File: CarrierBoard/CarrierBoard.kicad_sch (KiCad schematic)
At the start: 5 parts, among them J1 5-520315-4, J2 5-520315-6, J3 5-520315-8, J4 05JQ-BT, J5 09JQ-BT

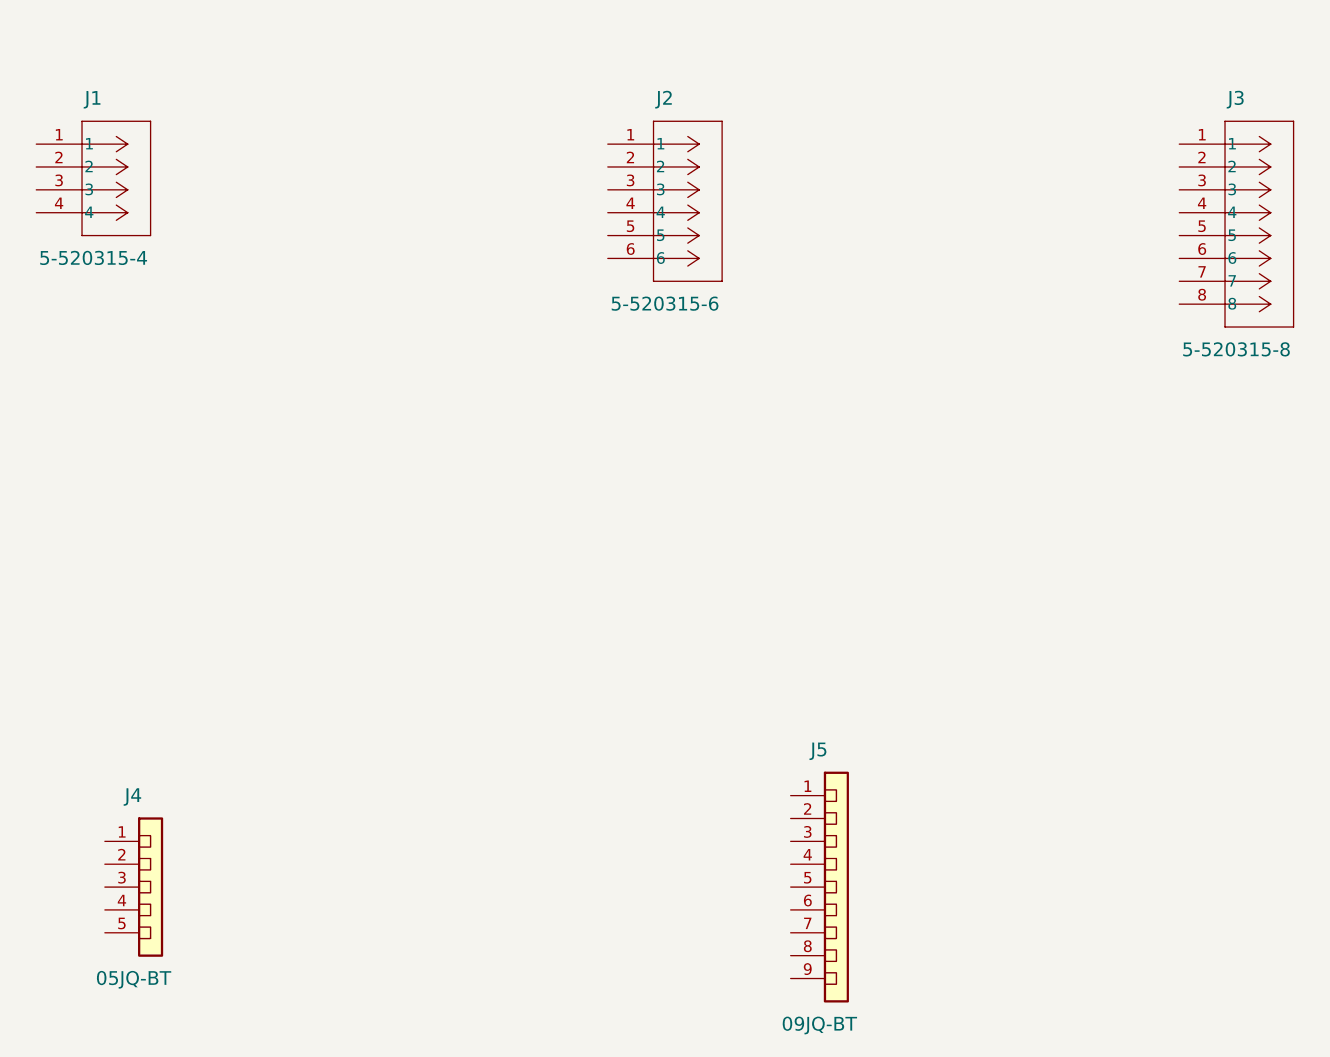
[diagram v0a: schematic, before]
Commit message: power flags
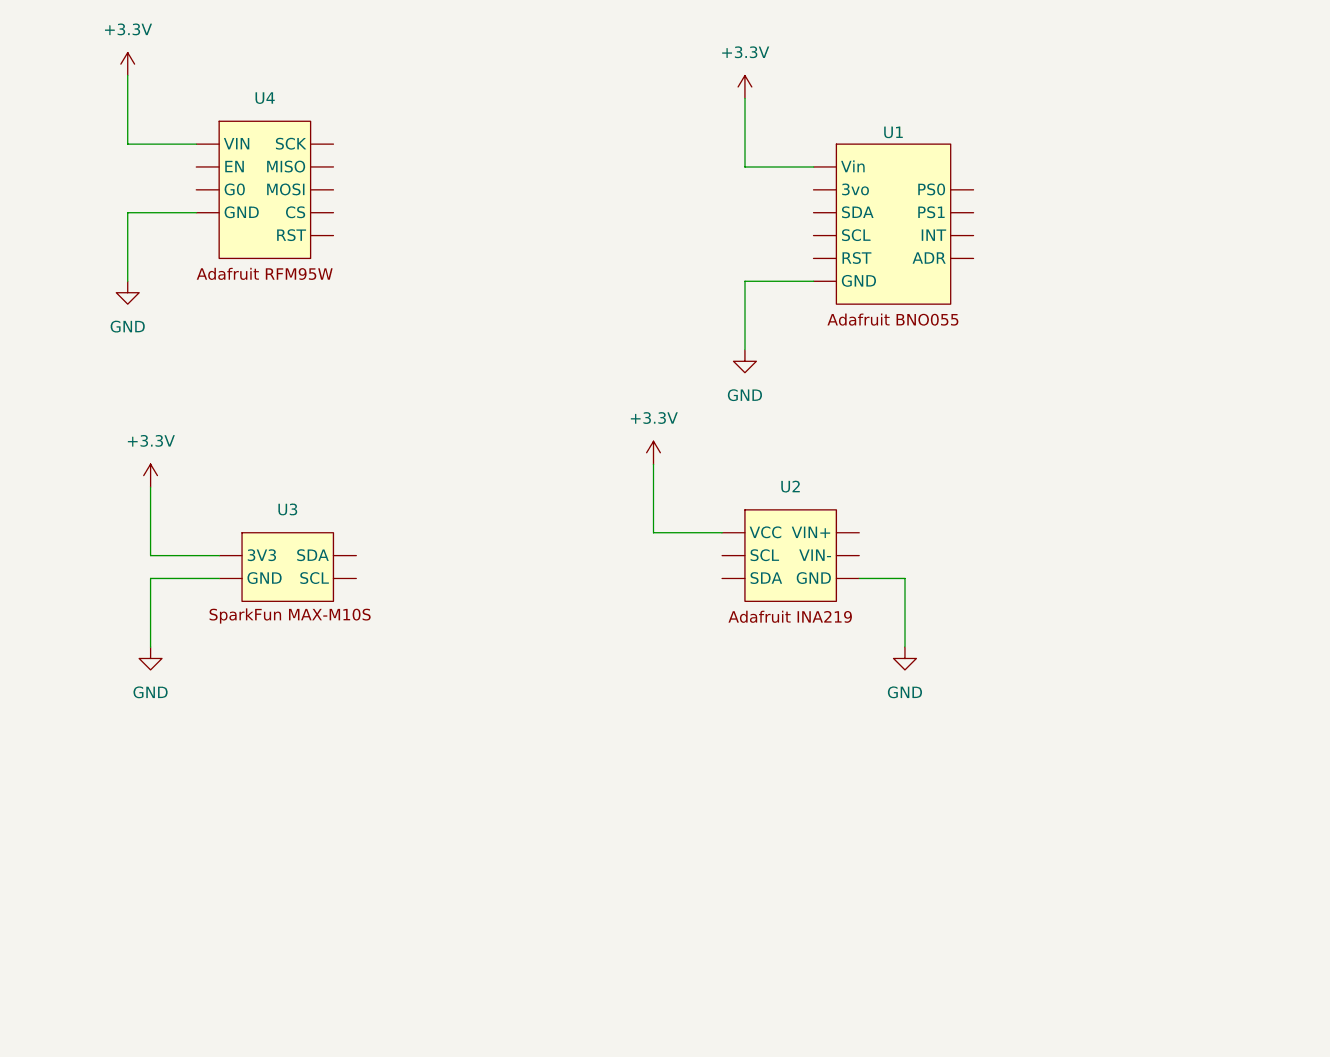
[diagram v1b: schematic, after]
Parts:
- removed J1: 5-520315-4, CarrierBoard:CONN_5-520315-4_TYC, symbol CarrierBoard:5-520315-4
- removed J2: 5-520315-6, CarrierBoard:CONN6X1_5-520315-6_TEC, symbol CarrierBoard:5-520315-6
- removed J3: 5-520315-8, CarrierBoard:CONN_5-520315-8_TYC, symbol CarrierBoard:5-520315-8
- removed J4: 05JQ-BT, CarrierBoard:JST_05JQ-BT_1x05_P2.50mm_Vertical, symbol CarrierBoard:05JQ-BT
- removed J5: 09JQ-BT, CarrierBoard:JST_09JQ-BT_1x09_P2.50mm_Vertical, symbol CarrierBoard:09JQ-BT
- added U1: (no value), symbol CarrierBoard:Adafruit BNO055 MillMax Pins
- added U2: (no value), symbol CarrierBoard:Adafruit_INA219
- added U3: (no value), symbol CarrierBoard:SparkFun_GNSS_Receiver_MAX-M10S
- added U4: (no value), symbol CarrierBoard:Adafruit_RFM95W
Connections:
- new net +3.3V: U1.1 (Vin), U2.1 (VCC), U3.2 (3V3), U4.1 (VIN)
- new net GND: U1.3 (GND), U2.2 (GND), U3.1 (GND), U4.2 (GND)
